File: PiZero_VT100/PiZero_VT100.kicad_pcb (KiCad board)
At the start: 2 copper layers, 99.7 x 99.9 mm, 24 parts, among them J1 GPIO, J2 RS232, J3 Ext. Power max,. 9V DC/AC, J4 Mini-DIN-6, J5 to Testpins 22(DM) and TP23(D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, J6 USB_A, J7 Z80-MBC2 direct, U2 LM7805_TO220

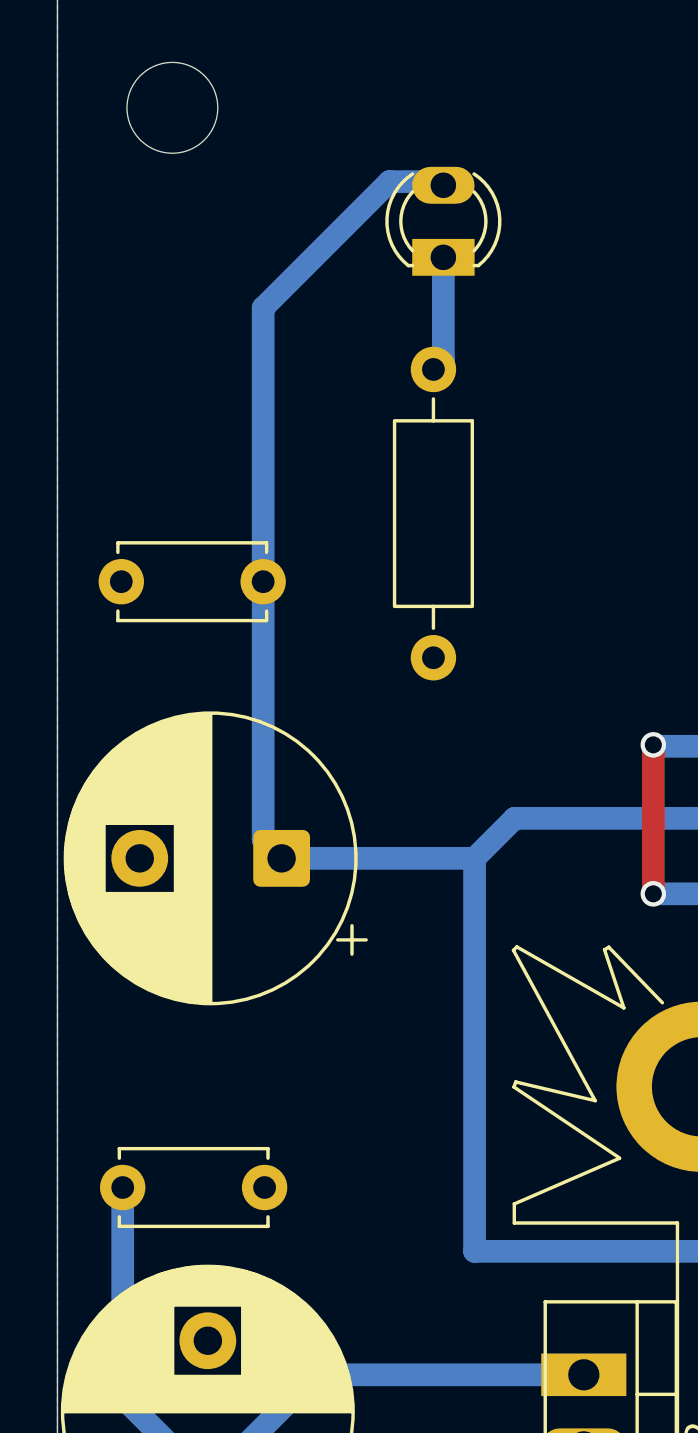
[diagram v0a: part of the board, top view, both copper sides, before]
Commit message: Adapterplatine überarbeitet
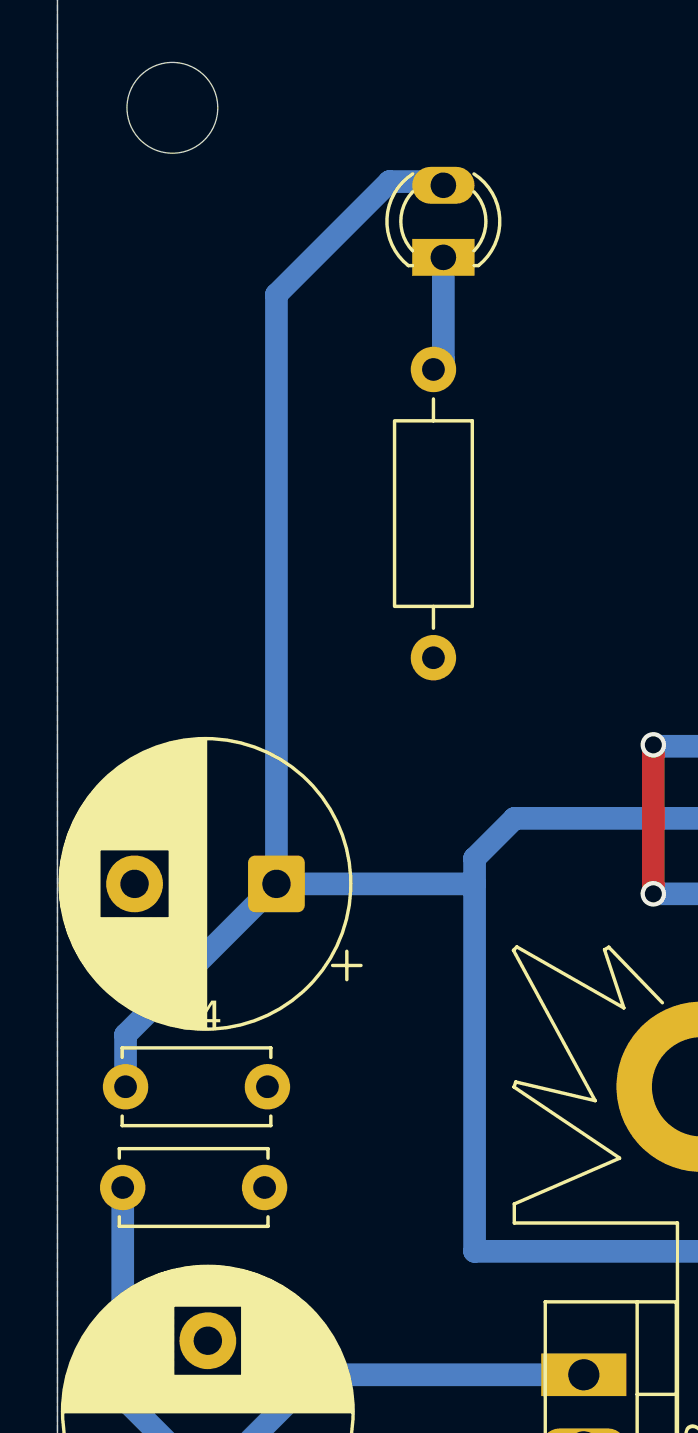
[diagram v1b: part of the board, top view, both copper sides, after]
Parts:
- moved C4 18.4 mm to (101.6, 107.4), turned to 0 degrees
- moved C3 0.92 mm to (106.9, 100.2)
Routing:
- net +5V: track 136.6 -> 146.6 mm

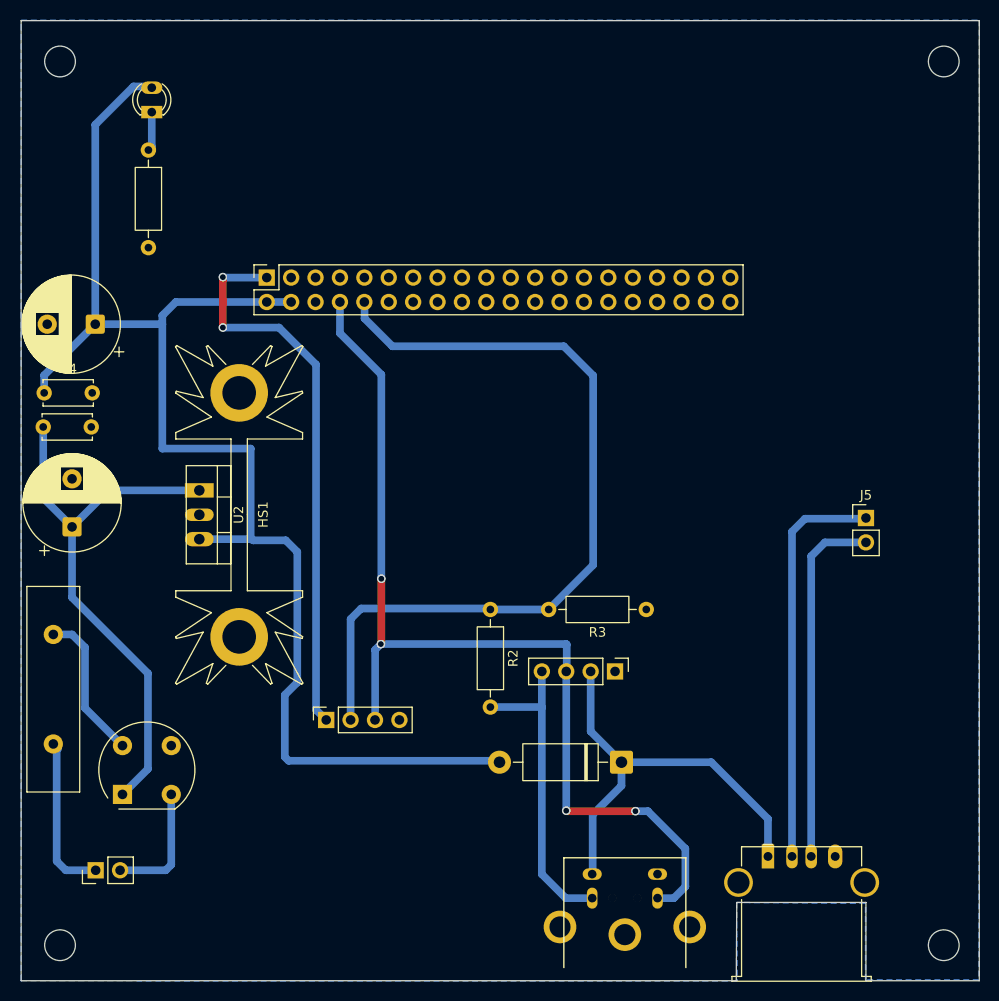
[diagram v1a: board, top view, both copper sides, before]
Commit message: Schaltung aktualisiert Umschaltung RxD <> TxD fehlt noch
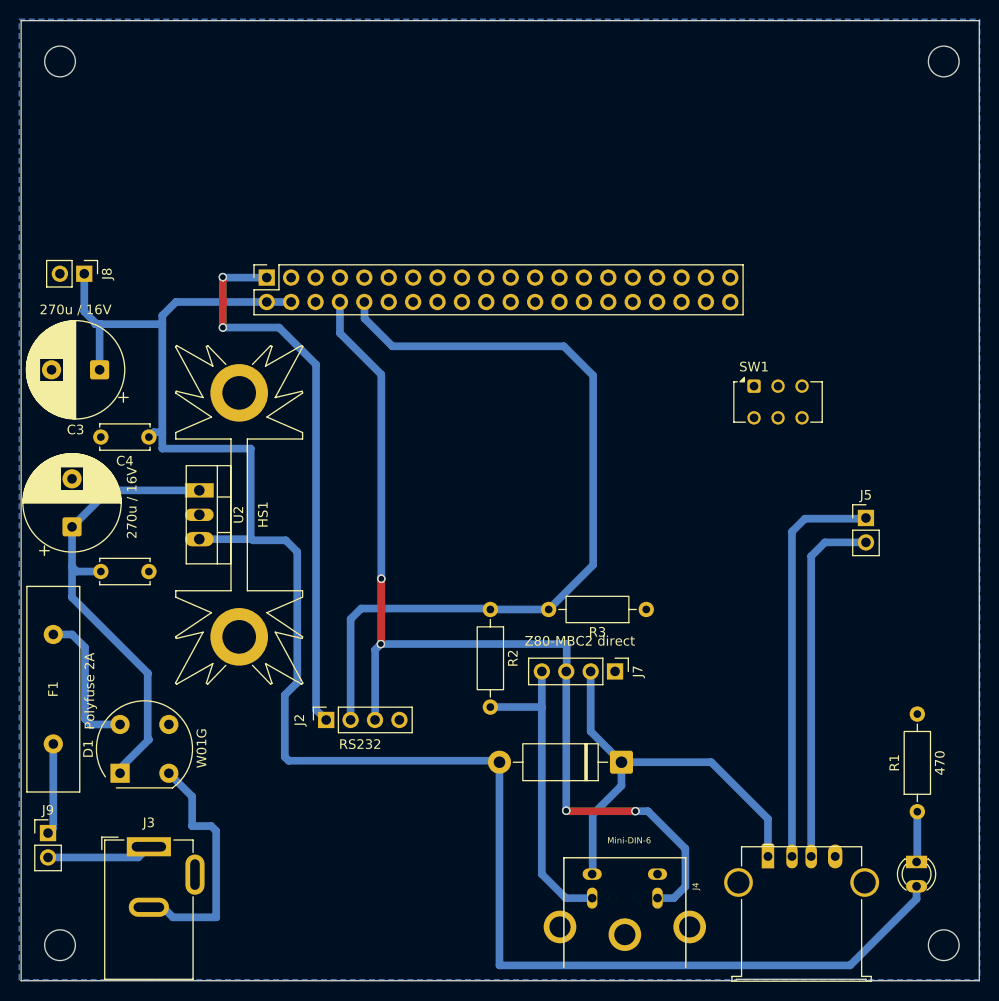
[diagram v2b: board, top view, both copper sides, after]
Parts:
- added J8: LCD Power, Connector_PinHeader_2.54mm:PinHeader_1x02_P2.54mm_Vertical, F.Cu at (105.8, 95.0)
- added J9: On / Off, Connector_PinHeader_2.54mm:PinHeader_1x02_P2.54mm_Vertical, F.Cu at (102.0, 153.2)
- added SW1: RXD <> TxD, Button_Switch_THT:SW_CK_JS202011AQN_DPDT_Angled, F.Cu at (175.5, 106.7)
- F1: value Polyfuse 1A -> Polyfuse 2A
- J3: footprint Connector_PinHeader_2.54mm:PinHeader_1x02_P2.54mm_Vertical -> Connector_BarrelJack:BarrelJack_GCT_DCJ200-10-A_Horizontal
- moved D2 111.5 mm to (192.4, 156.2), turned to -90 degrees
- moved R1 105.6 mm to (192.5, 151.0), turned to 90 degrees
- moved C2 16.2 mm to (107.5, 126.0)
- moved C4 11.8 mm to (112.5, 112.0), turned to 180 degrees
- moved J3 6.06 mm to (112.5, 154.7), turned to 0 degrees
- moved C3 4.77 mm to (107.4, 105.0)
- moved D1 2.21 mm to (109.5, 147.0)
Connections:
- F1 pad 1: Net-(J3-In) -> Net-(J9-Pin_1)
- J2 pad 2: /GPIO15/RXD0 -> Net-(J2-Pin_2)
- J2 pad 3: /GPIO14/TXD0 -> Net-(J2-Pin_3)
- J4 pad 3: /GPIO14/TXD0 -> Net-(J2-Pin_3)
- J7 pad 3: /GPIO14/TXD0 -> Net-(J2-Pin_3)
- R2 pad 1: /GPIO15/RXD0 -> Net-(J2-Pin_2)
- R3 pad 2: /GPIO15/RXD0 -> Net-(J2-Pin_2)
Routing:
- net +5V: track 146.6 -> 190.0 mm
- net Net-(J3-Ext): track 12.9 -> 25.6 mm
- net Net-(D1-+): track 58.7 -> 48.3 mm
- net Net-(J9-Pin_1): track 0.00 -> 10.00 mm
- net Net-(J3-In): track 17.5 -> 11.0 mm
- net Net-(D2-K): track 4.09 -> 5.26 mm
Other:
- outline, holes or cut-outs redrawn

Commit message: Umschalter TxD / RxD über Relais
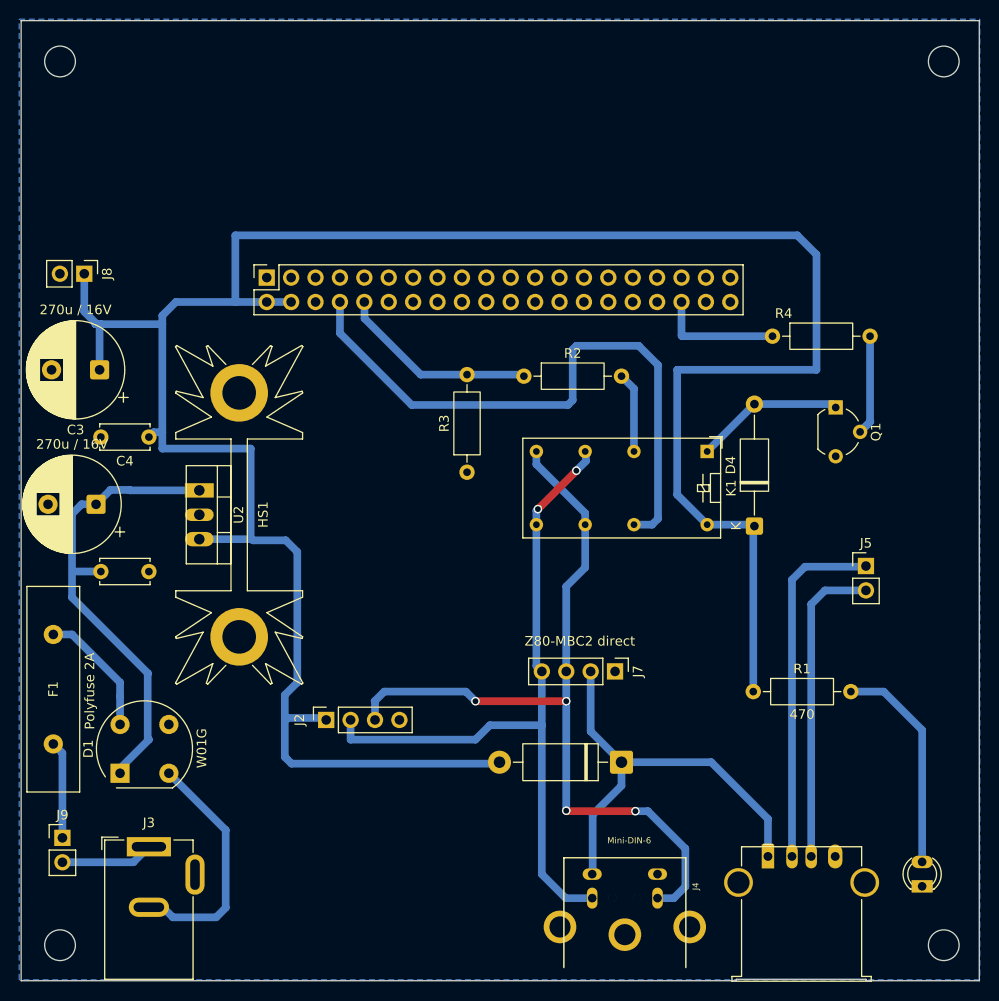
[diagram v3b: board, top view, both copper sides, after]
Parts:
- removed SW1: RXD <> TxD, Button_Switch_THT:SW_CK_JS202011AQN_DPDT_Angled
- added D4: 1N4148, Diode_THT:D_A-405_P12.70mm_Horizontal, F.Cu at (175.5, 121.3)
- added K1: G5V-2, Relay_THT:Relay_DPDT_Omron_G5V-2, F.Cu at (170.6, 113.5)
- added Q1: BC547, Package_TO_SOT_THT:TO-92_Wide, F.Cu at (184.0, 108.9)
- added R4: 1k, Resistor_THT:R_Axial_DIN0207_L6.3mm_D2.5mm_P10.16mm_Horizontal, F.Cu at (177.4, 101.5)
- moved R2 24.5 mm to (151.5, 105.7), turned to 0 degrees
- moved R3 23.5 mm to (145.6, 115.7), turned to 90 degrees
- moved R1 21.2 mm to (175.4, 138.5), turned to 0 degrees
- moved J5 5.00 mm to (187.2, 125.4)
- moved C1 3.43 mm to (107.0, 119.0), turned to 180 degrees
- moved D2 2.61 mm to (193.0, 158.8), turned to 90 degrees
- moved J9 1.58 mm to (103.5, 153.7)
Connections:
- D2 pad 1: Net-(D2-K) -> GND
- D2 pad 2: +5V -> Net-(D2-A)
- J2 pad 1: +3V3 -> +5V
- J4 pad 4: Net-(J7-Pin_4) -> Net-(J2-Pin_2)
- J7 pad 4: Net-(J7-Pin_4) -> Net-(J2-Pin_2)
- R1 pad 1: Net-(D2-K) -> +5V
- R1 pad 2: GND -> Net-(D2-A)
- R2 pad 1: Net-(J2-Pin_2) -> /GPIO15/RXD0
- R2 pad 2: Net-(J7-Pin_4) -> Net-(K1-Pad4)
- R3 pad 2: Net-(J2-Pin_2) -> /GPIO15/RXD0
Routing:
- net Net-(J2-Pin_3): track 0.00 -> 84.4 mm, vias 0 -> 4
- net Net-(J2-Pin_2): track 0.00 -> 75.2 mm, vias 0 -> 2
- net +5V: track 190.0 -> 260.5 mm
- net /GPIO15/RXD0: track 86.0 -> 20.9 mm
- net +3V3: track 58.6 -> 0.00 mm, vias 2 -> 0
- net /GPIO14/TXD0: track 103.6 -> 64.7 mm, vias 4 -> 0
- net Net-(J7-Pin_4): track 32.8 -> 0.00 mm
- net Net-(D2-A): track 0.00 -> 22.9 mm
- net Net-(D4-A): track 0.00 -> 16.0 mm
- net /GPIO16: track 0.00 -> 13.0 mm
- net Net-(Q1-B): track 0.00 -> 11.3 mm
- net Net-(K1-Pad4): track 0.00 -> 8.38 mm
- net Net-(D2-K): track 5.26 -> 0.00 mm
- net Net-(J5-Pin_2): track 37.6 -> 32.6 mm
- net Net-(J5-Pin_1): track 42.1 -> 37.1 mm
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
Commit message: aktualisierung des Status
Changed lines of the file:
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@@
-	)
-	(segment
-		(start 108.5 117.5)
-		(end 110.5 117.5)
-		(width 0.8)
-		(layer "B.Cu")
-		(net 35)
-	)
-	(segment
-		(start 110.55 117.55)
-		(end 117.75 117.55)
-		(width 0.8)
-		(layer "B.Cu")
-		(net 35)
-	)
-	(segment
-		(start 107 119)
-		(end 108.5 117.5)
-		(width 0.8)
-		(layer "B.Cu")
-		(net 35)
 	)
 	(segment
@@
 	(segment
 		(start 107 119)
+		(end 108.45 117.55)
+		(width 0.8)
+		(layer "B.Cu")
+		(net 35)
+	)
+	(segment
+		(start 107 119)
 		(end 105.5 119)
 		(width 0.8)
@@
 	)
 	(segment
-		(start 110.5 117.5)
-		(end 110.55 117.55)
-		(width 0.8)
-		(layer "B.Cu")
-		(net 35)
-	)
-	(segment
 		(start 112.379 136.621)
 		(end 112.379 143.379)
@@
 	)
 	(segment
+		(start 108.45 117.55)
+		(end 117.75 117.55)
+		(width 0.8)
+		(layer "B.Cu")
+		(net 35)
+	)
+	(segment
 		(start 112.379 143.379)
 		(end 112.5 143.5)
@@
 	)
 	(segment
-		(start 163.15 150.95)
+		(start 164.45 150.95)
 		(end 156 150.95)
 		(width 0.8)
@@
 	)
 	(via
-		(at 163.15 150.95)
+		(at 164.45 150.95)
 		(size 0.9)
 		(drill 0.6)
@@
 	)
 	(segment
+		(start 164.45 150.95)
+		(end 168.35 154.85)
+		(width 0.8)
+		(layer "B.Cu")
+		(net 49)
+	)
+	(segment
 		(start 137 138.5)
 		(end 136 139.5)
@@
 	)
 	(segment
-		(start 163.15 150.95)
-		(end 164.45 150.95)
-		(width 0.8)
-		(layer "B.Cu")
-		(net 49)
-	)
-	(segment
 		(start 145.5 138.5)
 		(end 137 138.5)
@@
 	)
 	(segment
+		(start 168.35 154.85)
+		(end 168.35 158.8)
+		(width 0.8)
+		(layer "B.Cu")
+		(net 49)
+	)
+	(segment
 		(start 146.5 139.5)
 		(end 145.5 138.5)
@@
 	)
 	(segment
-		(start 164.45 150.95)
-		(end 168.35 154.85)
-		(width 0.8)
-		(layer "B.Cu")
-		(net 49)
-	)
-	(segment
-		(start 168.35 154.85)
-		(end 168.35 158.8)
-		(width 0.8)
-		(layer "B.Cu")
-		(net 49)
-	)
-	(segment
 		(start 152.84 114.84)
 		(end 157.92 119.92)
@@
 	)
 	(segment
+		(start 155.95 136.4)
+		(end 155.95 139.5)
+		(width 0.8)
+		(layer "B.Cu")
+		(net 49)
+	)
+	(segment
+		(start 152.84 113.5)
+		(end 152.84 114.84)
+		(width 0.8)
+		(layer "B.Cu")
+		(net 49)
+	)
+	(segment
+		(start 167.15 160)
+		(end 165.45 160)
+		(width 0.8)
+		(layer "B.Cu")
+		(net 49)
+	)
+	(segment
 		(start 168.35 158.8)
 		(end 167.15 160)
 		(width 0.8)
 		(layer "B.Cu")
-		(net 49)
-	)
-	(segment
-		(start 155.95 136.4)
-		(end 155.95 139.5)
-		(width 0.8)
-		(layer "B.Cu")
-		(net 49)
-	)
-	(segment
-		(start 152.84 113.5)
-		(end 152.84 114.84)
-		(width 0.8)
-		(layer "B.Cu")
-		(net 49)
-	)
-	(segment
-		(start 167.15 160)
-		(end 165.45 160)
-		(width 0.8)
-		(layer "B.Cu")

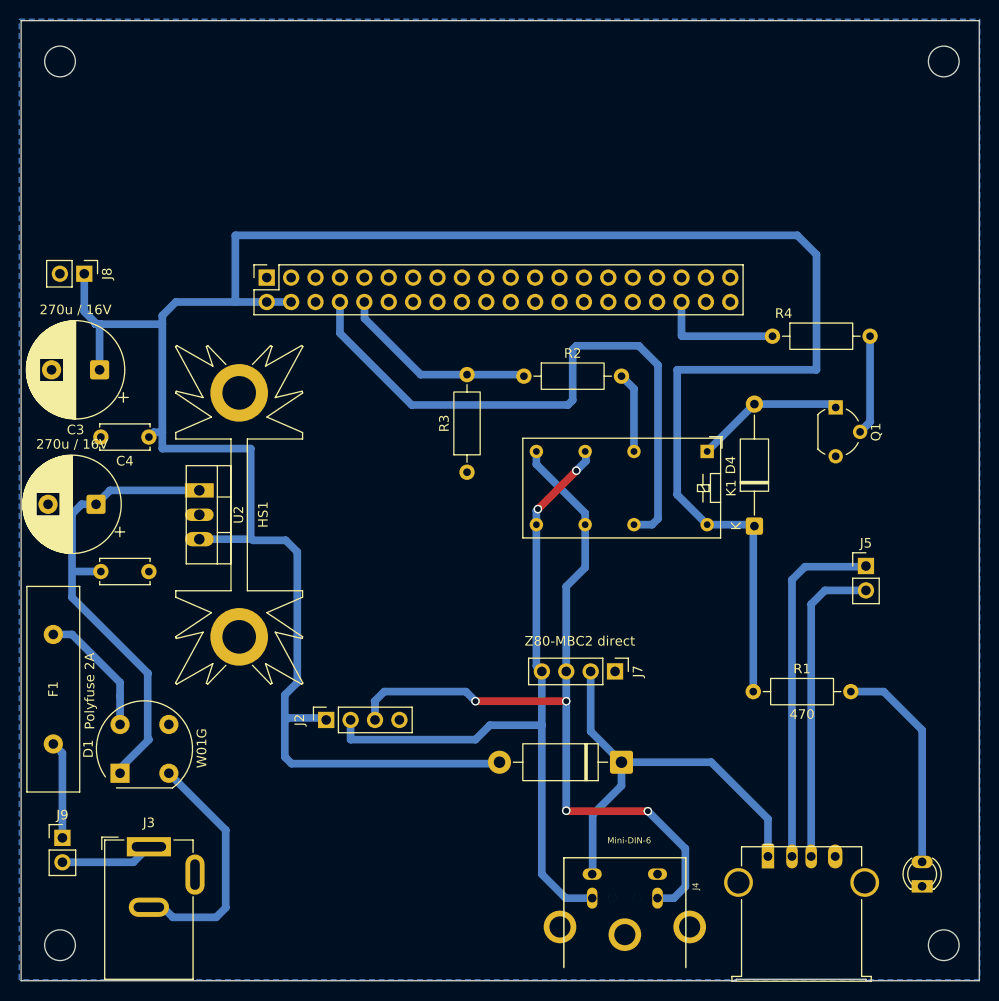
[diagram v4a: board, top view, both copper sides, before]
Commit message: LM350 eingebaut in Design
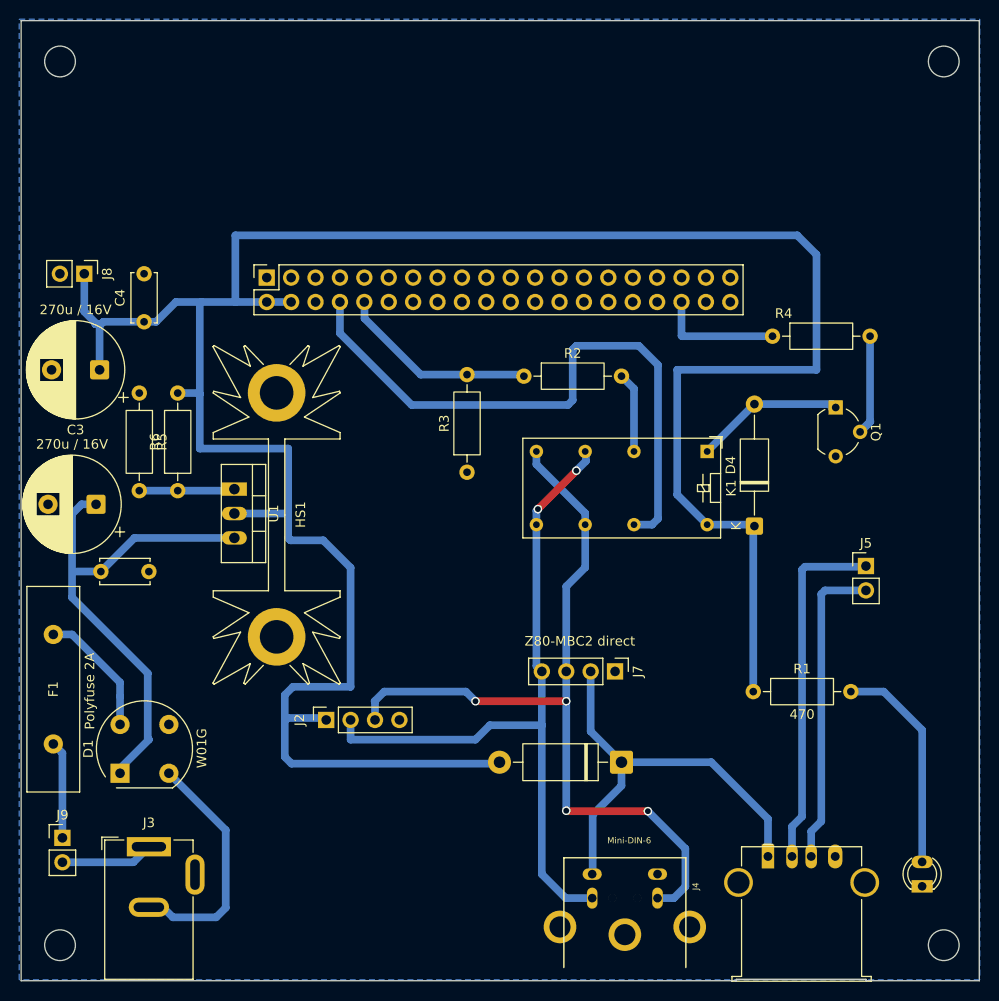
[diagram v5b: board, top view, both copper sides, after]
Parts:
- removed U2: LM7805_TO220, Package_TO_SOT_THT:TO-220-3_Vertical
- added R5: 720, Resistor_THT:R_Axial_DIN0207_L6.3mm_D2.5mm_P10.16mm_Horizontal, F.Cu at (111.5, 107.4)
- added R6: 240, Resistor_THT:R_Axial_DIN0207_L6.3mm_D2.5mm_P10.16mm_Horizontal, F.Cu at (115.5, 117.6)
- added U1: LM350_TO220, Package_TO_SOT_THT:TO-220-3_Vertical, F.Cu at (121.4, 117.4)
- HS1: value Heatsink_Pad_2Pin -> 6 K/W
- moved C4 12.0 mm to (112.0, 100.0), turned to 90 degrees
- moved HS1 3.90 mm to (125.8, 120.1)
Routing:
- net Net-(U1-ADJ): track 0.00 -> 9.97 mm
- net +5V: track 260.5 -> 269.6 mm
- net Net-(D1-+): track 48.3 -> 52.3 mm
